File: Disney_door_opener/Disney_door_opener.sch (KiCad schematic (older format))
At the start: 30 parts, among them J1 Screw_Terminal_01x02, J2 Conn_01x02, J3 Conn_01x02, J4 Conn_01x05, J5 Screw_Terminal_01x02, J6 Conn_01x15, J7 Conn_01x15, U1 LM2596S-5, U3 MAX98357A

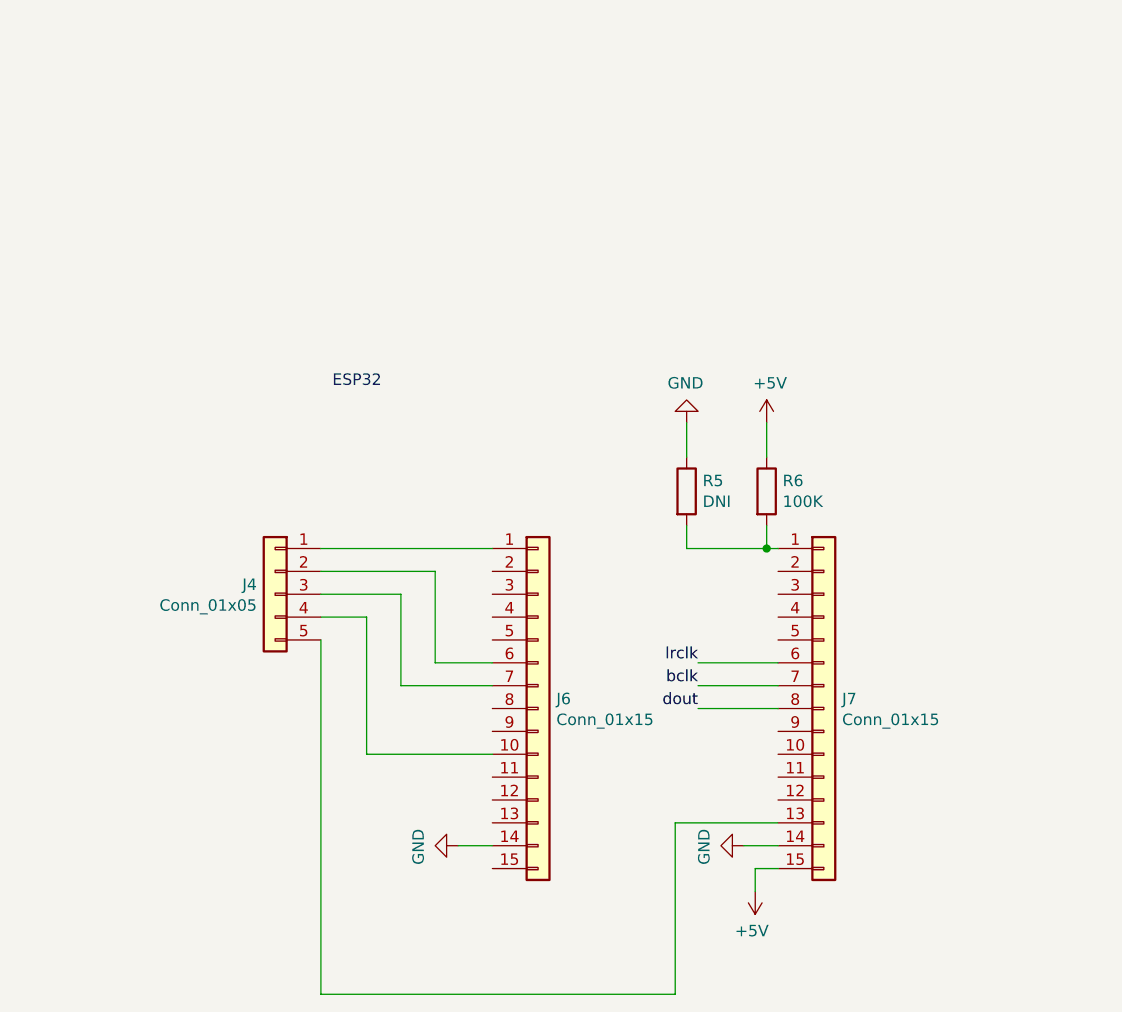
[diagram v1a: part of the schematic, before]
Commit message: Corrected swapped pins.
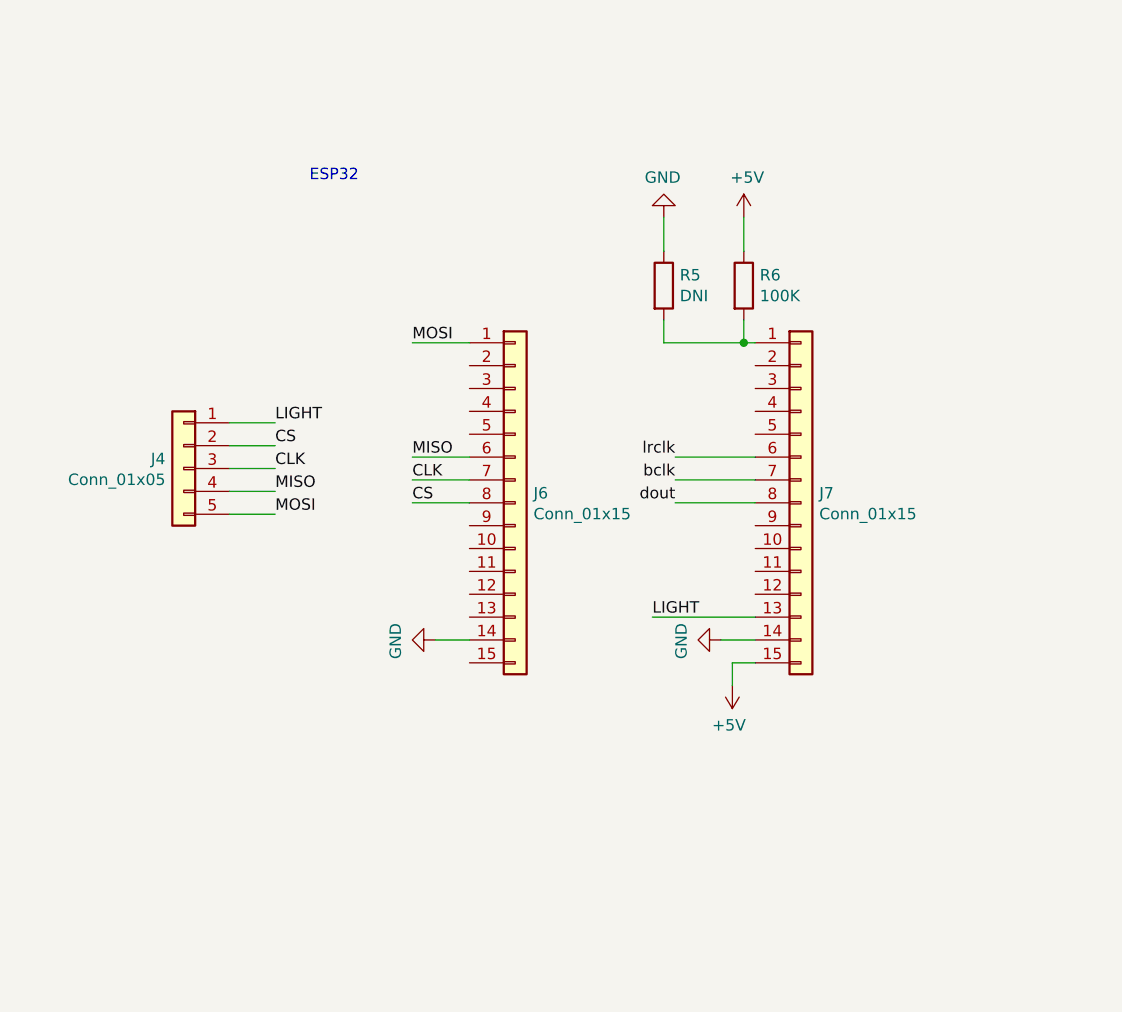
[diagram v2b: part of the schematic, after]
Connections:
- net LIGHT: now reaches J4.1 (Pin_1)
- net LIGHT: now also J7.13 (Pin_13); no longer J6.1 (Pin_1)
- net CS: now reaches J4.2 (Pin_2)
- net CS: now also J6.8 (Pin_8); no longer J6.6 (Pin_6)
- net CLK: now reaches J4.3 (Pin_3), J6.7 (Pin_7)
- net at J6.10 (Pin_10): no longer J4.4 (Pin_4)
- net MOSI: now reaches J4.5 (Pin_5)
- net MOSI: now also J6.1 (Pin_1); no longer J7.13 (Pin_13)
- new net MISO: J4.4 (Pin_4), J6.6 (Pin_6)
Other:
- moved on the sheet: J4, J6, J7, R5, R6
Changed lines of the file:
@@
 L Connector_Generic:Conn_01x15 J6
 U 1 1 6485E55E
-P 2700 5700
-F 0 "J6" H 2780 5742 50  0000 L CNN
-F 1 "Conn_01x15" H 2780 5651 50  0000 L CNN
-F 2 "Connector_PinHeader_2.54mm:PinHeader_1x15_P2.54mm_Vertical" H 2700 5700 50  0001 C CNN
-F 3 "~" H 2700 5700 50  0001 C CNN
-	1    2700 5700
+P 2600 4800
+F 0 "J6" H 2680 4842 50  0000 L CNN
+F 1 "Conn_01x15" H 2680 4751 50  0000 L CNN
+F 2 "Connector_PinHeader_2.54mm:PinHeader_1x15_P2.54mm_Vertical" H 2600 4800 50  0001 C CNN
+F 3 "~" H 2600 4800 50  0001 C CNN
+	1    2600 4800
 	1    0    0    -1
 $EndComp
@@
 L Connector_Generic:Conn_01x15 J7
 U 1 1 6487741E
-P 3950 5700
-F 0 "J7" H 4030 5742 50  0000 L CNN
-F 1 "Conn_01x15" H 4030 5651 50  0000 L CNN
-F 2 "Connector_PinHeader_2.54mm:PinHeader_1x15_P2.54mm_Vertical" H 3950 5700 50  0001 C CNN
-F 3 "~" H 3950 5700 50  0001 C CNN
-	1    3950 5700
+P 3850 4800
+F 0 "J7" H 3930 4842 50  0000 L CNN
+F 1 "Conn_01x15" H 3930 4751 50  0000 L CNN
+F 2 "Connector_PinHeader_2.54mm:PinHeader_1x15_P2.54mm_Vertical" H 3850 4800 50  0001 C CNN
+F 3 "~" H 3850 4800 50  0001 C CNN
+	1    3850 4800
 	1    0    0    -1
 $EndComp
 Wire Wire Line
-	3750 5000 3700 5000
+	3650 4100 3600 4100
 Wire Wire Line
-	3750 5500 3400 5500
-Text Label 3400 5500 2    50   ~ 0
+	3650 4600 3300 4600
+Text Label 3300 4600 2    50   ~ 0
 lrclk
 Wire Wire Line
-	3750 5600 3400 5600
-Text Label 3400 5600 2    50   ~ 0
+	3650 4700 3300 4700
+Text Label 3300 4700 2    50   ~ 0
 bclk
-Text Label 3400 5700 2    50   ~ 0
+Text Label 3300 4800 2    50   ~ 0
 dout
 Wire Wire Line
-	3750 5700 3400 5700
+	3650 4800 3300 4800
 Wire Wire Line
-	3750 6200 3300 6200
+	3650 5300 3200 5300
 Wire Wire Line
-	3300 6200 3300 6950
-Wire Wire Line
-	3650 6400 3650 6500
+	3550 5500 3550 5600
 $Comp
 L power:+5V #PWR0129
 U 1 1 648ADAEA
-P 3650 6500
-F 0 "#PWR0129" H 3650 6350 50  0001 C CNN
-F 1 "+5V" H 3665 6673 50  0000 C CNN
-F 2 "" H 3650 6500 50  0001 C CNN
-F 3 "" H 3650 6500 50  0001 C CNN
-	1    3650 6500
+P 3550 5600
+F 0 "#PWR0129" H 3550 5450 50  0001 C CNN
+F 1 "+5V" H 3565 5773 50  0000 C CNN
+F 2 "" H 3550 5600 50  0001 C CNN
+F 3 "" H 3550 5600 50  0001 C CNN
+	1    3550 5600
 	-1   0    0    1
 $EndComp
 Wire Wire Line
-	3750 6400 3650 6400
+	3650 5500 3550 5500
 Wire Wire Line
-	3750 6300 3600 6300
+	3650 5400 3500 5400
 $Comp
 L power:GND #PWR0124
 U 1 1 648B90AC
-P 3600 6300
-F 0 "#PWR0124" H 3600 6050 50  0001 C CNN
-F 1 "GND" H 3605 6127 50  0000 C CNN
-F 2 "" H 3600 6300 50  0001 C CNN
-F 3 "" H 3600 6300 50  0001 C CNN
-	1    3600 6300
+P 3500 5400
+F 0 "#PWR0124" H 3500 5150 50  0001 C CNN
+F 1 "GND" H 3505 5227 50  0000 C CNN
+F 2 "" H 3500 5400 50  0001 C CNN
+F 3 "" H 3500 5400 50  0001 C CNN
+	1    3500 5400
 	0    1    1    0
 $EndComp
 Wire Wire Line
-	2500 6300 2350 6300
+	2400 5400 2250 5400
 $Comp
 L power:GND #PWR0125
 U 1 1 648BD950
-P 2350 6300
-F 0 "#PWR0125" H 2350 6050 50  0001 C CNN
-F 1 "GND" H 2355 6127 50  0000 C CNN
-F 2 "" H 2350 6300 50  0001 C CNN
-F 3 "" H 2350 6300 50  0001 C CNN
-	1    2350 6300
+P 2250 5400
+F 0 "#PWR0125" H 2250 5150 50  0001 C CNN
+F 1 "GND" H 2255 5227 50  0000 C CNN
+F 2 "" H 2250 5400 50  0001 C CNN
+F 3 "" H 2250 5400 50  0001 C CNN
+	1    2250 5400
 	0    1    1    0
 $EndComp
 Wire Wire Line
-	3700 4600 3700 4450
+	3600 3700 3600 3550
 Wire Wire Line
-	3350 4450 3350 4600
+	3250 3550 3250 3700
 $Comp
 L power:GND #PWR0128
 U 1 1 64741E63
-P 3350 4450
-F 0 "#PWR0128" H 3350 4200 50  0001 C CNN
-F 1 "GND" H 3355 4277 50  0000 C CNN
-F 2 "" H 3350 4450 50  0001 C CNN
-F 3 "" H 3350 4450 50  0001 C CNN
-	1    3350 4450
+P 3250 3550
+F 0 "#PWR0128" H 3250 3300 50  0001 C CNN
+F 1 "GND" H 3255 3377 50  0000 C CNN
+F 2 "" H 3250 3550 50  0001 C CNN
+F 3 "" H 3250 3550 50  0001 C CNN
+	1    3250 3550
 	-1   0    0    1
 $EndComp
@@
 L power:+5V #PWR0127
 U 1 1 64741E5D
-P 3700 4450
-F 0 "#PWR0127" H 3700 4300 50  0001 C CNN
-F 1 "+5V" H 3715 4623 50  0000 C CNN
-F 2 "" H 3700 4450 50  0001 C CNN
-F 3 "" H 3700 4450 50  0001 C CNN
-	1    3700 4450
+P 3600 3550
+F 0 "#PWR0127" H 3600 3400 50  0001 C CNN
+F 1 "+5V" H 3615 3723 50  0000 C CNN
+F 2 "" H 3600 3550 50  0001 C CNN
+F 3 "" H 3600 3550 50  0001 C CNN
+	1    3600 3550
 	1    0    0    -1
 $EndComp
 Wire Wire Line
-	3350 5000 3350 4900
+	3250 4100 3250 4000
 Wire Wire Line
-	3700 5000 3350 5000
+	3600 4100 3250 4100
 Wire Wire Line
-	3700 5000 3700 4900
+	3600 4100 3600 4000
 $Comp
 L Device:R R5
 U 1 1 64741E52
-P 3350 4750
-F 0 "R5" H 3420 4796 50  0000 L CNN
-F 1 "DNI" H 3420 4705 50  0000 L CNN
-F 2 "Resistor_SMD:R_1206_3216Metric_Pad1.30x1.75mm_HandSolder" V 3280 4750 50  0001 C CNN
-F 3 "~" H 3350 4750 50  0001 C CNN
-	1    3350 4750
+P 3250 3850
+F 0 "R5" H 3320 3896 50  0000 L CNN
+F 1 "DNI" H 3320 3805 50  0000 L CNN
+F 2 "Resistor_SMD:R_1206_3216Metric_Pad1.30x1.75mm_HandSolder" V 3180 3850 50  0001 C CNN
+F 3 "~" H 3250 3850 50  0001 C CNN
+	1    3250 3850
 	1    0    0    -1
 $EndComp
@@
 L Device:R R6
 U 1 1 64741E4C
-P 3700 4750
-F 0 "R6" H 3770 4796 50  0000 L CNN
-F 1 "100K" H 3770 4705 50  0000 L CNN
-F 2 "Resistor_SMD:R_1206_3216Metric_Pad1.30x1.75mm_HandSolder" V 3630 4750 50  0001 C CNN
-F 3 "~" H 3700 4750 50  0001 C CNN
-	1    3700 4750
+P 3600 3850
+F 0 "R6" H 3670 3896 50  0000 L CNN
+F 1 "100K" H 3670 3805 50  0000 L CNN
+F 2 "Resistor_SMD:R_1206_3216Metric_Pad1.30x1.75mm_HandSolder" V 3530 3850 50  0001 C CNN
+F 3 "~" H 3600 3850 50  0001 C CNN
+	1    3600 3850
 	1    0    0    -1
 $EndComp
-Connection ~ 3700 5000
+Connection ~ 3600 4100
 $Comp
 L Connector_Generic:Conn_01x05 J4
 U 1 1 646F431E
-P 1550 5200
-F 0 "J4" H 1630 5242 50  0000 L CNN
-F 1 "Conn_01x05" H 1630 5151 50  0000 L CNN
-F 2 "Connector_PinHeader_2.54mm:PinHeader_1x05_P2.54mm_Vertical" H 1550 5200 50  0001 C CNN
-F 3 "~" H 1550 5200 50  0001 C CNN
-	1    1550 5200
+P 1150 4650
+F 0 "J4" H 1230 4692 50  0000 L CNN
+F 1 "Conn_01x05" H 1230 4601 50  0000 L CNN
+F 2 "Connector_PinHeader_2.54mm:PinHeader_1x05_P2.54mm_Vertical" H 1150 4650 50  0001 C CNN
+F 3 "~" H 1150 4650 50  0001 C CNN
+	1    1150 4650
 	-1   0    0    -1
 $EndComp
 Wire Wire Line
-	1750 5000 2500 5000
-Wire Wire Line
-	2250 5500 2250 5100
-Wire Wire Line
-	2250 5100 1750 5100
-Wire Wire Line
-	2250 5500 2500 5500
-Wire Wire Line
-	2100 5600 2100 5200
-Wire Wire Line
-	2100 5200 1750 5200
-Wire Wire Line
-	1950 5900 1950 5300
-Wire Wire Line
-	1950 5300 1750 5300
-Wire Wire Line
-	2100 5600 2500 5600
-Wire Wire Line
-	1950 5900 2500 5900
-Wire Wire Line
-	1750 6950 1750 5400
-Wire Wire Line
-	1750 6950 3300 6950
-Text Notes 1800 4300 0    50   ~ 0
+	2150 4600 2400 4600
+Text Notes 1700 3400 0    50   ~ 0
 ESP32\n
 $Comp
@@
 	-1   0    0    1
 $EndComp
+Wire Wire Line
+	1350 4850 1550 4850
+Wire Wire Line
+	1350 4750 1550 4750
+Wire Wire Line
+	1350 4650 1550 4650
+Wire Wire Line
+	1350 4550 1550 4550
+Wire Wire Line
+	1350 4450 1550 4450
+Wire Wire Line
+	2400 4100 2150 4100
+Text Label 2150 4100 0    50   ~ 0
+MOSI
+Text Label 1550 4450 0    50   ~ 0
+LIGHT
+Text Label 1550 4550 0    50   ~ 0
+CS
+Text Label 1550 4650 0    50   ~ 0
+CLK
+Text Label 1550 4750 0    50   ~ 0
+MISO
+Text Label 1550 4850 0    50   ~ 0
+MOSI
+Text Label 2150 4600 0    50   ~ 0
+MISO
+Wire Wire Line
+	2400 4700 2150 4700
+Text Label 2150 4700 0    50   ~ 0
+CLK
+Wire Wire Line
+	2400 4800 2150 4800
+Text Label 2150 4800 0    50   ~ 0
+CS
+Text Label 3200 5300 0    50   ~ 0
+LIGHT
 $EndSCHEMATC

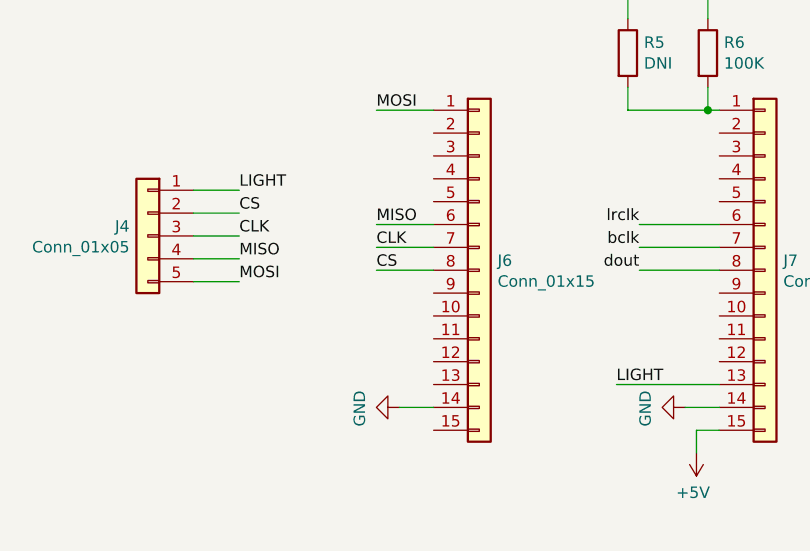
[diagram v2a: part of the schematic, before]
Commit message: Minor corrections. Changed pin headers to female.
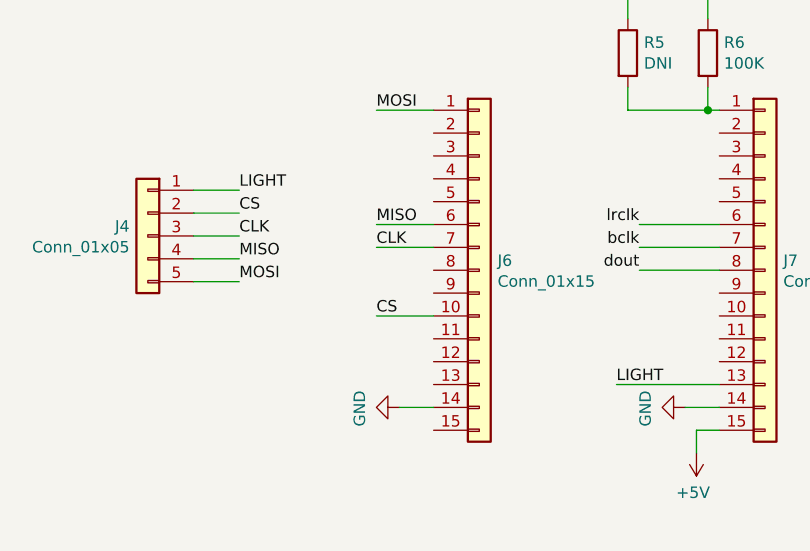
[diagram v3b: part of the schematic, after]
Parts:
- J6, J7: footprint Connector_PinHeader_2.54mm:PinHeader_1x15_P2.54mm_Vertical -> Connector_PinSocket_2.54mm:PinSocket_1x15_P2.54mm_Vertical
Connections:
- net CS: now also J6.10 (Pin_10); no longer J6.8 (Pin_8)
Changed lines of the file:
@@
 F 0 "J6" H 2680 4842 50  0000 L CNN
 F 1 "Conn_01x15" H 2680 4751 50  0000 L CNN
-F 2 "Connector_PinHeader_2.54mm:PinHeader_1x15_P2.54mm_Vertical" H 2600 4800 50  0001 C CNN
+F 2 "Connector_PinSocket_2.54mm:PinSocket_1x15_P2.54mm_Vertical" H 2600 4800 50  0001 C CNN
 F 3 "~" H 2600 4800 50  0001 C CNN
 	1    2600 4800
@@
 F 0 "J7" H 3930 4842 50  0000 L CNN
 F 1 "Conn_01x15" H 3930 4751 50  0000 L CNN
-F 2 "Connector_PinHeader_2.54mm:PinHeader_1x15_P2.54mm_Vertical" H 3850 4800 50  0001 C CNN
+F 2 "Connector_PinSocket_2.54mm:PinSocket_1x15_P2.54mm_Vertical" H 3850 4800 50  0001 C CNN
 F 3 "~" H 3850 4800 50  0001 C CNN
 	1    3850 4800
@@
 CLK
 Wire Wire Line
-	2400 4800 2150 4800
-Text Label 2150 4800 0    50   ~ 0
+	2400 5000 2150 5000
+Text Label 2150 5000 0    50   ~ 0
 CS
 Text Label 3200 5300 0    50   ~ 0
